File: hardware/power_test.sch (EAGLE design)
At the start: 53 parts, among them J10 USB-MICROA-AMPHENOL-10118192-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, J3 USB-MICROB-EDAC-690-005-299-0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, U1 DPDT-X2, U2 3.3V, U3 FT232RLSSOP, U4 MCP73831T-2ACI/OT, Y1 P-FET

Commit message: smaller caps
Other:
- note added: "If we follow the example of both sparkfun and adafruit, this nonsense with the fet is not necessary. The data sheet claims VBAT will never fall below 3.7V."
- note added: "Things to check: 1. Does the FTDI LDO 3.3V regulator work when VBUS is at 3.7V? 2. Can we keep current below 50mA for the microcontroller, etc. ? The question, I guess is LEDs: ucontrller says it draws < 18.6mA. Redboard does fine, but FTDI gets a little hot."
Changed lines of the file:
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@@
 Selecting VBUS, powers the FTDI whenever USB is attached.
 Connecting all three will make USB attachment override the switch.</text>
+<text x="30.48" y="190.5" size="1.778" layer="97">If we follow the example of both sparkfun and adafruit, this nonsense with the fet is not necessary.
+The data sheet claims VBAT will never fall below 3.7V.</text>
+<text x="30.48" y="203.2" size="1.778" layer="97">Things to check:
+1.  Does the FTDI LDO 3.3V regulator work when VBUS is at 3.7V?
+2.  Can we keep current below 50mA for the microcontroller, etc. ?  The question, I guess is LEDs:  ucontrller says it draws &lt; 18.6mA.  Redboard does fine, but FTDI gets a little hot.
+</text>
 </plain>
 <instances>

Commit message: adjust resistor values after some testing.  make GND an High-I net.
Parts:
- R6, R7: value 1K -> 100; device quadparts_prebuilt:RESISTOR_SMD-2012-0805-1K -> quadparts_prebuilt:RESISTOR_SMD-2012-0805-100
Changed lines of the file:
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@@
 <part name="GND28" library="quadparts_prebuilt" deviceset="GND" device=""/>
 <part name="GND30" library="quadparts_prebuilt" deviceset="GND" device=""/>
-<part name="R6" library="quadparts_prebuilt" deviceset="RESISTOR_" device="SMD-2012-0805-1K" value="1K"/>
-<part name="R7" library="quadparts_prebuilt" deviceset="RESISTOR_" device="SMD-2012-0805-1K" value="1K"/>
+<part name="R6" library="quadparts_prebuilt" deviceset="RESISTOR_" device="SMD-2012-0805-100" value="100"/>
+<part name="R7" library="quadparts_prebuilt" deviceset="RESISTOR_" device="SMD-2012-0805-100" value="100"/>
 <part name="JP1" library="RemoteParts" deviceset="M06" device="-TH-RIGHT-ANGLE"/>
 <part name="C11" library="quadparts_prebuilt" deviceset="CAPACITOR-NP_" device="SMD-2012-0805_CERAMIC-0.1UF" value="0.1uF"/>
@@
 </busses>
 <nets>
-<net name="GND" class="0">
+<net name="GND" class="1">
 <segment>
 <pinref part="GND7" gate="1" pin="GND"/>

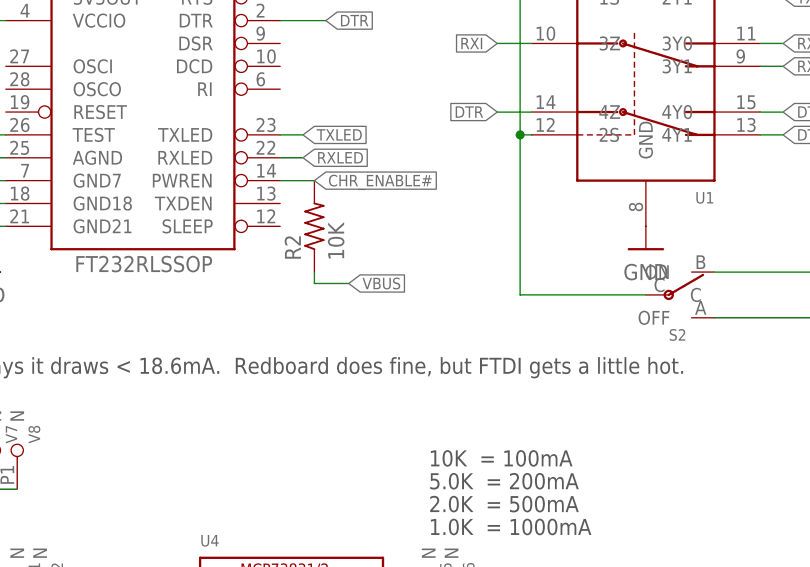
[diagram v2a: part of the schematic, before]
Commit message: Move pwren pull up to 3.3V rail in accordance with datasheet
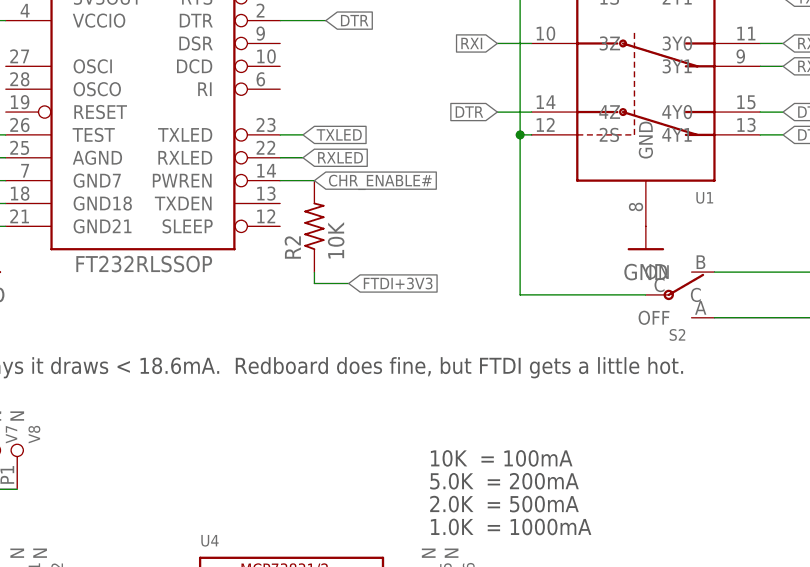
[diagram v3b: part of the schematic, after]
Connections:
- net FTDI+3V3: now also R2.1
- net VBUS: no longer R2.1
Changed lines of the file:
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@@
 <label x="96.52" y="146.05" size="1.27" layer="95" rot="R90" xref="yes"/>
+</segment>
+<segment>
+<pinref part="R2" gate="G$1" pin="1"/>
+<wire x1="187.96" y1="217.17" x2="187.96" y2="215.9" width="0.1524" layer="91"/>
+<wire x1="187.96" y1="215.9" x2="191.77" y2="215.9" width="0.1524" layer="91"/>
+<label x="191.77" y="215.9" size="1.27" layer="95" xref="yes"/>
 </segment>
 </net>
@@
 <label x="17.78" y="252.73" size="1.27" layer="95" rot="R270" xref="yes"/>
 </segment>
-<segment>
-<pinref part="R2" gate="G$1" pin="1"/>
-<wire x1="187.96" y1="217.17" x2="187.96" y2="215.9" width="0.1524" layer="91"/>
-<wire x1="187.96" y1="215.9" x2="191.77" y2="215.9" width="0.1524" layer="91"/>
-<label x="191.77" y="215.9" size="1.27" layer="95" xref="yes"/>
-</segment>
-</net>
+</net>

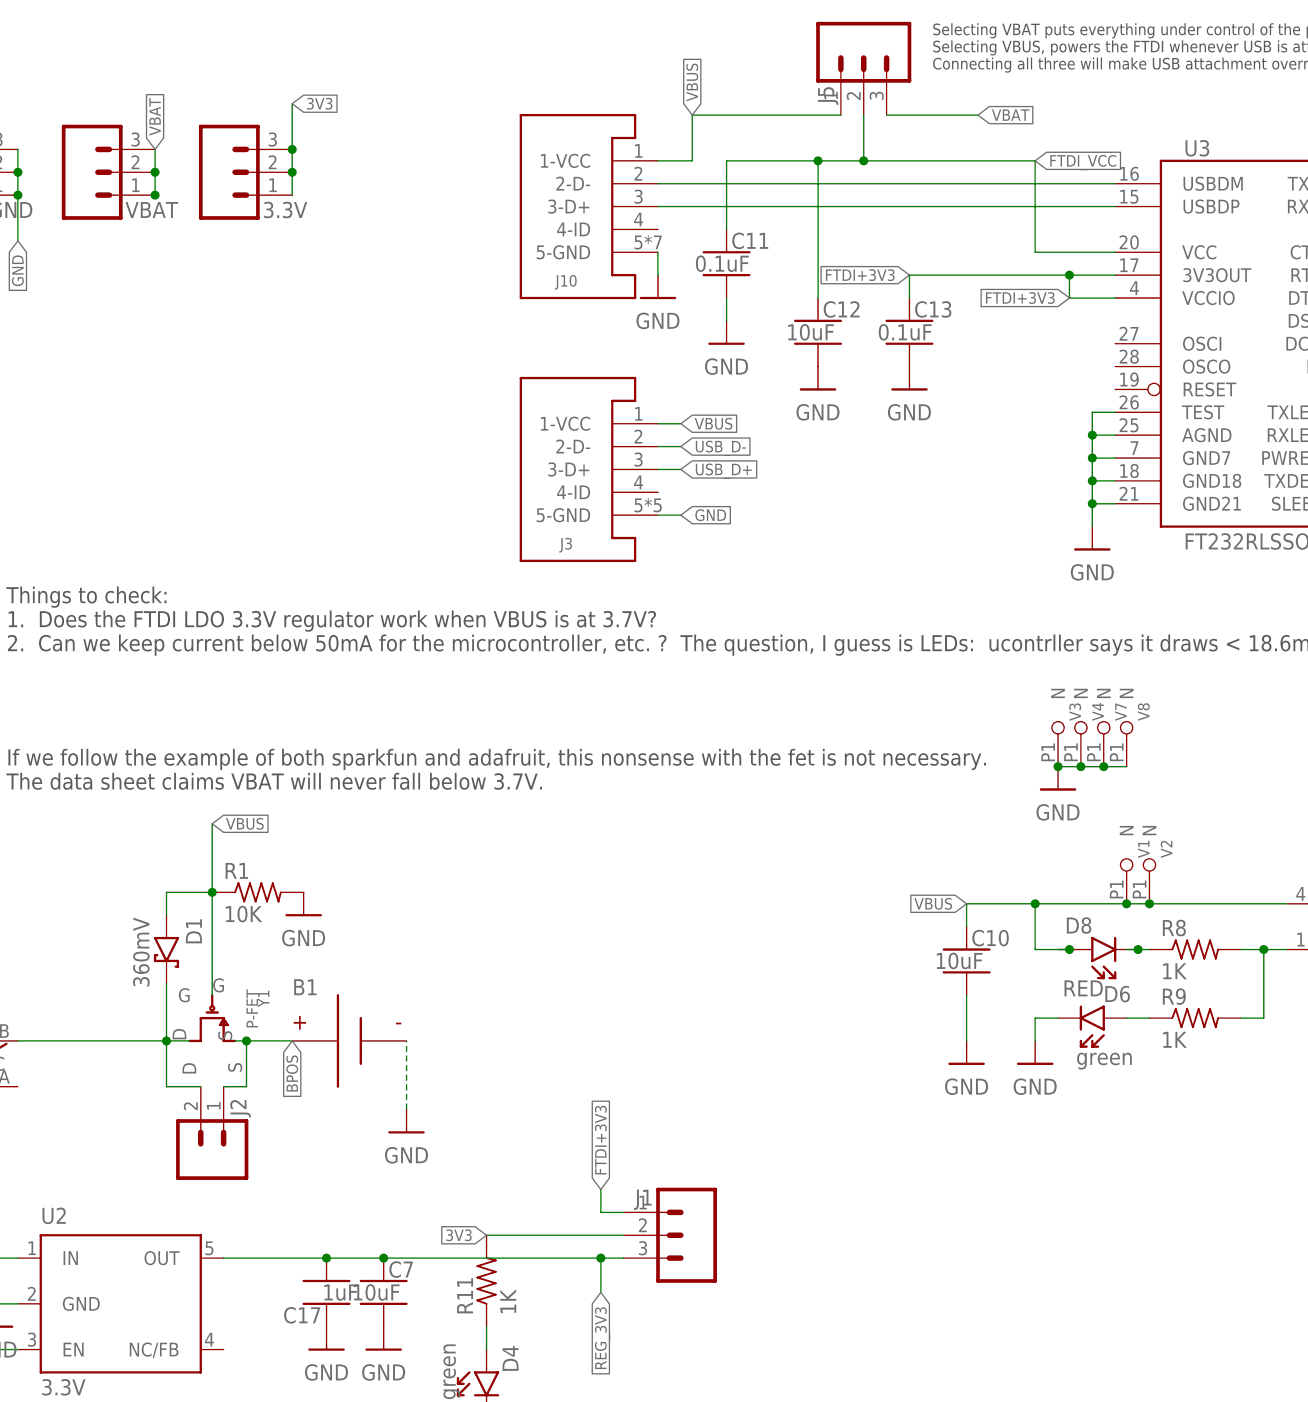
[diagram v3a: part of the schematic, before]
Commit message: Preliminary implementation of changes:
Connect VBUS to FTDI directly.
Connect FTDI regulator to 3.3V rail.
Remove mosfet, diode, short across J2.

Still needs clean up to remove uneeded jumpers.
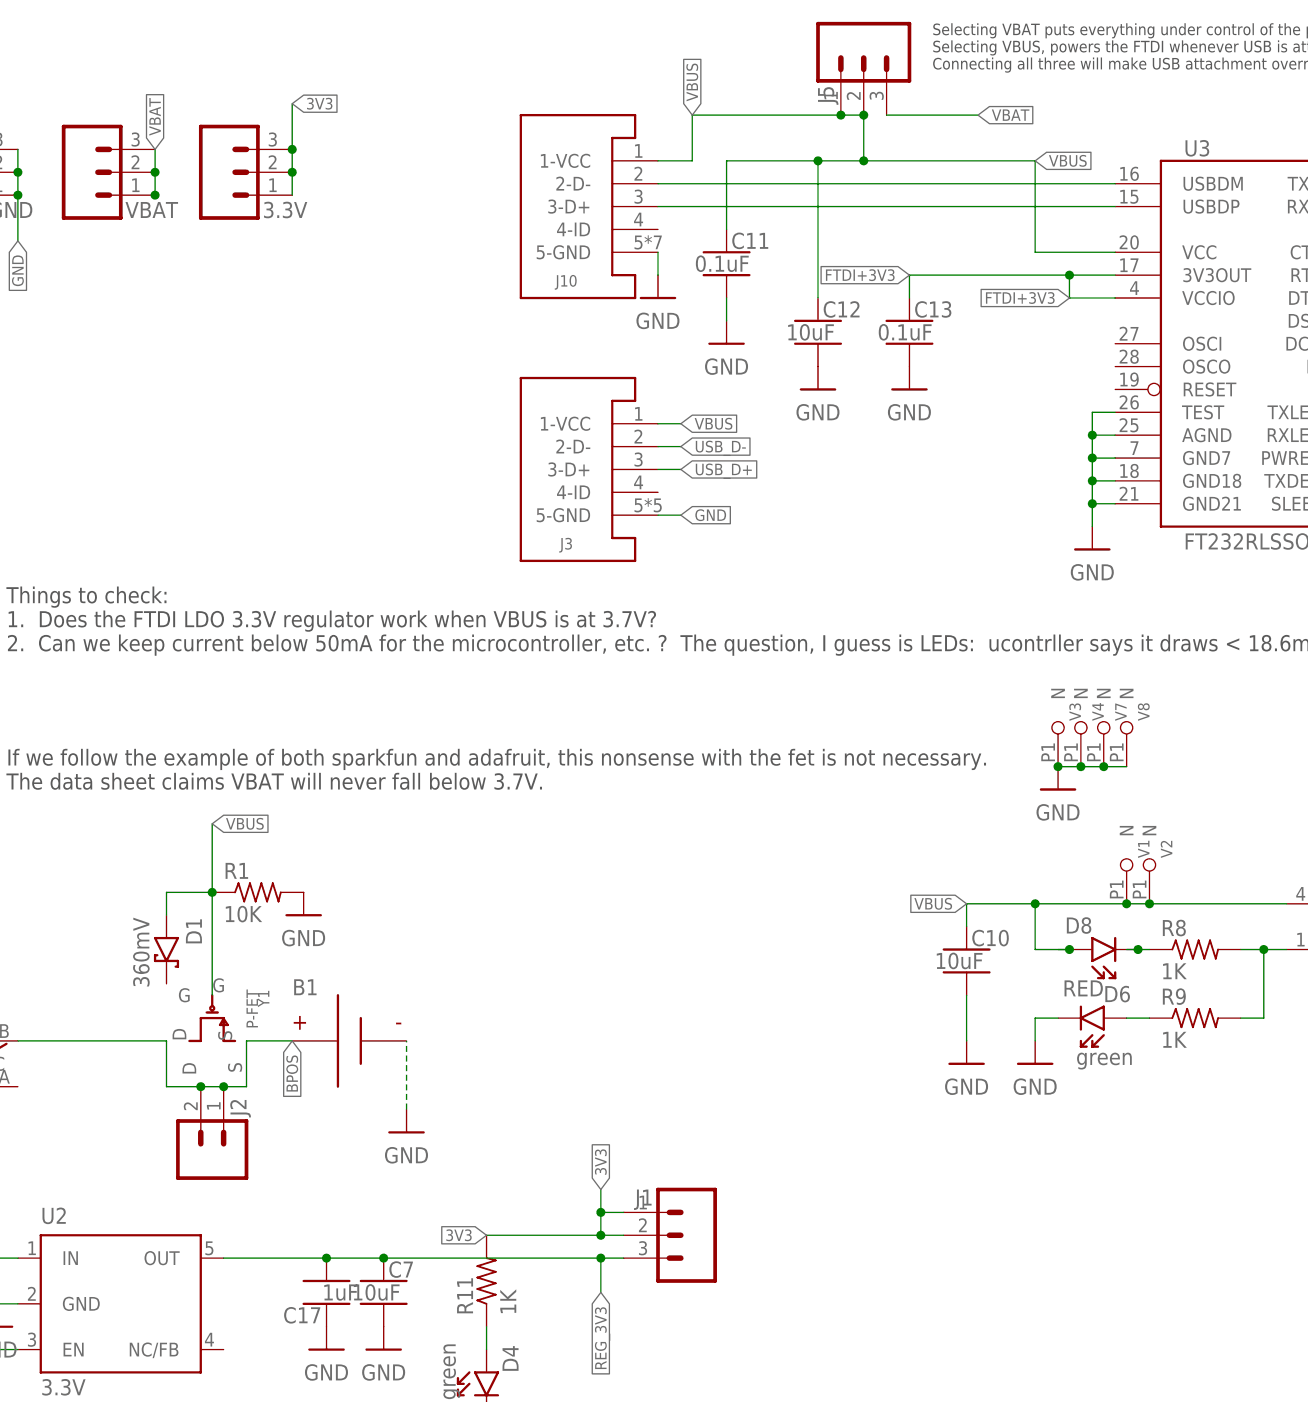
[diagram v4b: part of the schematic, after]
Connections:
- removed net FTDI_VCC: C11.1, C12.1, J5.2, U3.VCC
- removed net N$4: D1.C, J2.2, S1.ON, Y1.D
- net 3V3: now also J1.1
- net BPOS: now also J2.2, S1.ON; no longer Y1.S
- net FTDI+3V3: no longer J1.1
- net VBUS: now also C11.1, C12.1, J5.2, U3.VCC
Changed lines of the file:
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@@
 <setting verticaltext="up"/>
 </settings>
-<grid distance="0.1" unitdist="inch" unit="inch" style="lines" multiple="1" display="no" altdistance="0.01" altunitdist="inch" altunit="inch"/>
+<grid distance="0.05" unitdist="inch" unit="inch" style="lines" multiple="1" display="no" altdistance="0.01" altunitdist="inch" altunit="inch"/>
 <layers>
 <layer number="99" name="SpiceOrder" color="7" fill="1" visible="no" active="no"/>
@@
 </segment>
 <segment>
+<pinref part="J1" gate="G$1" pin="1"/>
+<wire x1="99.06" y1="143.51" x2="96.52" y2="143.51" width="0.1524" layer="91"/>
+<wire x1="96.52" y1="146.05" x2="96.52" y2="143.51" width="0.1524" layer="91"/>
+<label x="96.52" y="146.05" size="1.27" layer="95" rot="R90" xref="yes"/>
 <pinref part="J1" gate="G$1" pin="2"/>
 <label x="83.82" y="140.97" size="1.27" layer="95" rot="R180" xref="yes"/>
 <pinref part="R11" gate="G$1" pin="2"/>
-<wire x1="99.06" y1="140.97" x2="83.82" y2="140.97" width="0.1524" layer="91"/>
+<wire x1="99.06" y1="140.97" x2="96.52" y2="140.97" width="0.1524" layer="91"/>
+<wire x1="96.52" y1="140.97" x2="83.82" y2="140.97" width="0.1524" layer="91"/>
+<wire x1="96.52" y1="143.51" x2="96.52" y2="140.97" width="0.1524" layer="91"/>
+<junction x="96.52" y="143.51"/>
+<junction x="96.52" y="140.97"/>
 </segment>
 </net>
@@
 <segment>
 <pinref part="B1" gate="G$1" pin="P"/>
-<wire x1="55.88" y1="162.56" x2="57.15" y2="162.56" width="0.1524" layer="91"/>
 <label x="62.23" y="162.56" size="1.27" layer="95" rot="R270" xref="yes"/>
 <pinref part="J2" gate="G$1" pin="1"/>
@@
 <wire x1="57.15" y1="162.56" x2="57.15" y2="157.48" width="0.1524" layer="91"/>
 <wire x1="57.15" y1="157.48" x2="54.61" y2="157.48" width="0.1524" layer="91"/>
-<junction x="57.15" y="162.56"/>
-<pinref part="Y1" gate="G$1" pin="S"/>
+<pinref part="J2" gate="G$1" pin="2"/>
+<wire x1="48.26" y1="157.48" x2="52.07" y2="157.48" width="0.1524" layer="91"/>
+<wire x1="48.26" y1="162.56" x2="48.26" y2="157.48" width="0.1524" layer="91"/>
+<pinref part="S1" gate="G$1" pin="ON"/>
+<wire x1="31.75" y1="162.56" x2="48.26" y2="162.56" width="0.1524" layer="91"/>
+<wire x1="54.61" y1="157.48" x2="52.07" y2="157.48" width="0.1524" layer="91"/>
+<junction x="54.61" y="157.48"/>
+<junction x="52.07" y="157.48"/>
 </segment>
 </net>
@@
 </segment>
 <segment>
-<pinref part="J1" gate="G$1" pin="1"/>
-<wire x1="99.06" y1="143.51" x2="96.52" y2="143.51" width="0.1524" layer="91"/>
-<wire x1="96.52" y1="146.05" x2="96.52" y2="143.51" width="0.1524" layer="91"/>
-<label x="96.52" y="146.05" size="1.27" layer="95" rot="R90" xref="yes"/>
-</segment>
-<segment>
 <pinref part="R2" gate="G$1" pin="1"/>
 <wire x1="187.96" y1="217.17" x2="187.96" y2="215.9" width="0.1524" layer="91"/>
@@
 </segment>
 </net>
-<net name="FTDI_VCC" class="1">
-<segment>
+<net name="VBUS" class="1">
+<segment>
+<pinref part="J10" gate="A" pin="1-VCC"/>
+<wire x1="102.87" y1="260.35" x2="106.68" y2="260.35" width="0.1524" layer="91"/>
+<pinref part="J5" gate="G$1" pin="1"/>
+<wire x1="123.19" y1="265.43" x2="106.68" y2="265.43" width="0.1524" layer="91"/>
+<wire x1="106.68" y1="265.43" x2="106.68" y2="260.35" width="0.1524" layer="91"/>
+<label x="106.68" y="265.43" size="1.27" layer="95" rot="R90" xref="yes"/>
 <wire x1="110.49" y1="260.35" x2="120.65" y2="260.35" width="0.1524" layer="91"/>
 <wire x1="120.65" y1="260.35" x2="125.73" y2="260.35" width="0.1524" layer="91"/>
@@
 <junction x="125.73" y="260.35"/>
 <label x="144.78" y="260.35" size="1.27" layer="95" xref="yes"/>
-</segment>
-</net>
-<net name="VBUS" class="1">
-<segment>
-<pinref part="J10" gate="A" pin="1-VCC"/>
-<wire x1="102.87" y1="260.35" x2="106.68" y2="260.35" width="0.1524" layer="91"/>
-<pinref part="J5" gate="G$1" pin="1"/>
-<wire x1="123.19" y1="265.43" x2="106.68" y2="265.43" width="0.1524" layer="91"/>
-<wire x1="106.68" y1="265.43" x2="106.68" y2="260.35" width="0.1524" layer="91"/>
-<label x="106.68" y="265.43" size="1.27" layer="95" rot="R90" xref="yes"/>
+<wire x1="123.19" y1="265.43" x2="125.73" y2="265.43" width="0.1524" layer="91"/>
+<junction x="123.19" y="265.43"/>
+<junction x="125.73" y="265.43"/>
 </segment>
 <segment>
@@
 </segment>
 </net>
-<net name="N$4" class="1">
-<segment>
-<pinref part="J2" gate="G$1" pin="2"/>
-<wire x1="48.26" y1="157.48" x2="52.07" y2="157.48" width="0.1524" layer="91"/>
-<pinref part="Y1" gate="G$1" pin="D"/>
-<wire x1="48.26" y1="162.56" x2="50.8" y2="162.56" width="0.1524" layer="91"/>
-<wire x1="48.26" y1="162.56" x2="48.26" y2="157.48" width="0.1524" layer="91"/>
-<junction x="48.26" y="162.56"/>
-<pinref part="D1" gate="G$1" pin="C"/>
-<wire x1="48.26" y1="168.91" x2="48.26" y2="162.56" width="0.1524" layer="91"/>
-<pinref part="S1" gate="G$1" pin="ON"/>
-<wire x1="31.75" y1="162.56" x2="48.26" y2="162.56" width="0.1524" layer="91"/>
-</segment>
-</net>
